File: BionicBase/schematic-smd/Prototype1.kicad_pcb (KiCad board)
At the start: 2 copper layers, 114 x 102 mm, 15 parts, among them J1 Bionic_ZIF_Socket_48pin, SW1 Tact_SW, U1 TXS0108EPW, U2 TXS0108EPW, U3 TXS0108EPW, U4 TXS0108EPW, U5 TXS0108EPW

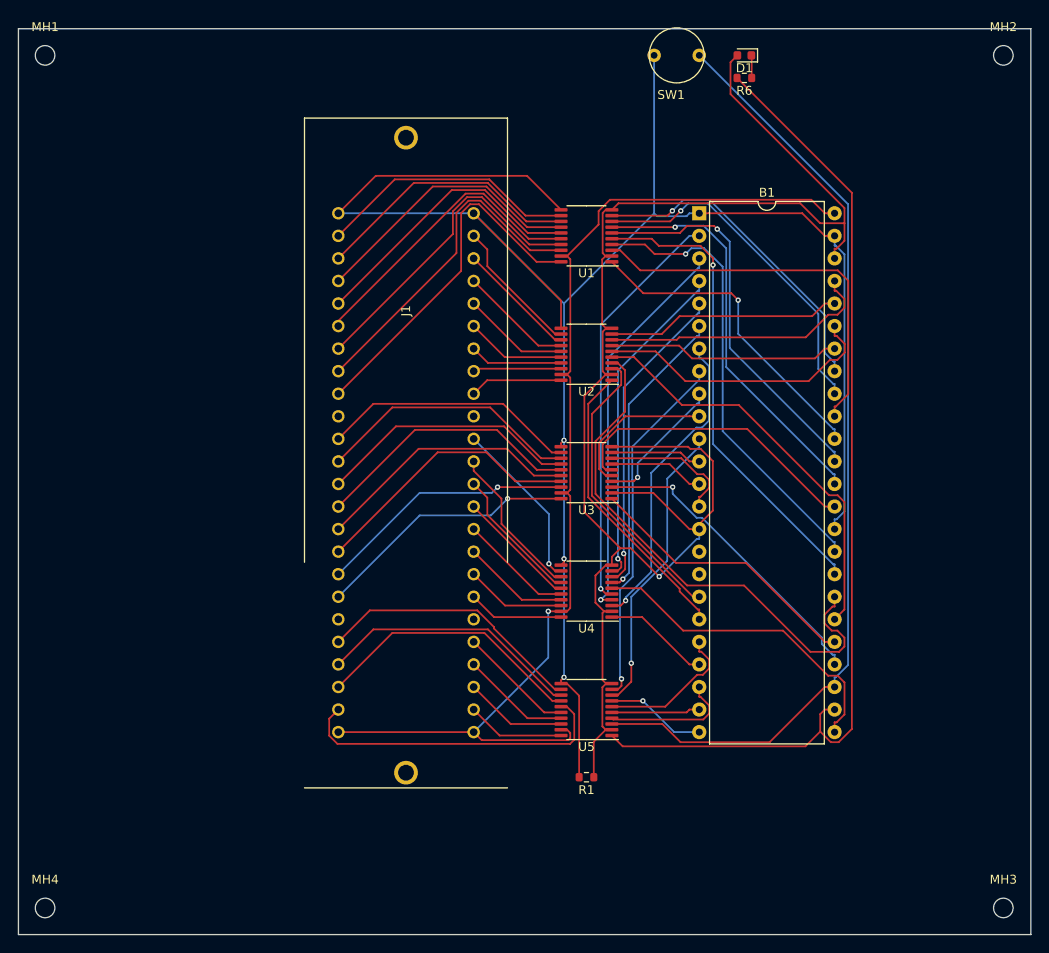
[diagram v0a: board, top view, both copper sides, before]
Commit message: [BionicBase] Add DC-DC Converter for +15V
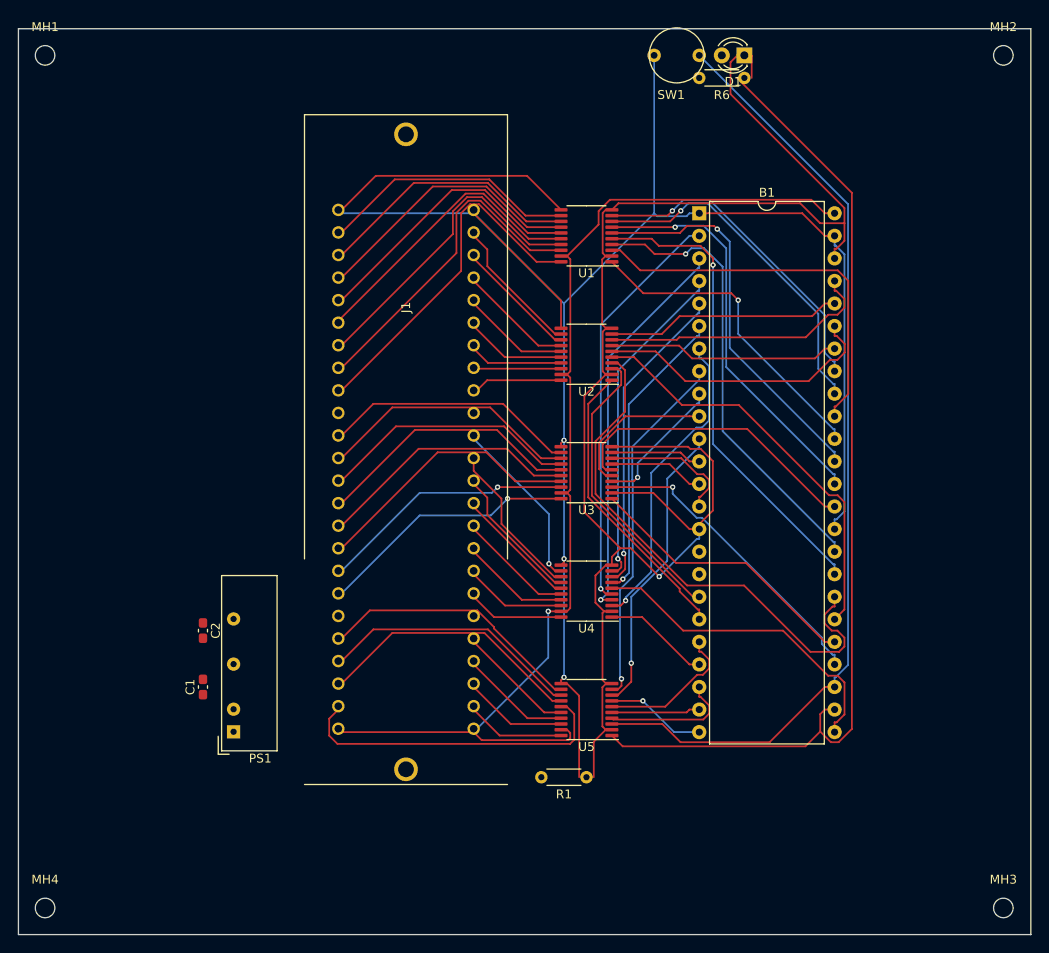
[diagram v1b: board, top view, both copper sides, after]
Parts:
- added C1: 2.2u, Capacitor_SMD:C_0603_1608Metric_Pad1.08x0.95mm_HandSolder, F.Cu at (93.4, 115.7)
- added C2: 1.0u, Capacitor_SMD:C_0603_1608Metric_Pad1.08x0.95mm_HandSolder, F.Cu at (93.4, 109.4)
- added PS1: MAU105, 0-LocalLibrary:Converter_DCDC_Minmax_MAU100_THT, F.Cu at (96.8, 120.8)
- D1: footprint LED_SMD:LED_0603_1608Metric -> LED_THT:LED_D3.0mm
- R1, R6: footprint Resistor_SMD:R_0603_1608Metric -> Resistor_THT:R_Axial_DIN0204_L3.6mm_D1.6mm_P5.08mm_Horizontal
- moved J1 0.38 mm to (116.2, 76.0)
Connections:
- net +3V3 renamed +3.3V
- J1 pad 19: unconnected-(J1-Pad19) -> /+15V
- J1 pad 30: unconnected-(J1-Pad30) -> /+15V
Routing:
- net (no net): track 0.00 -> 179.8 mm, vias 0 -> 1
- net +3.3V: track 177.2 -> 0.00 mm, vias 1 -> 0
- net Net-(D1-K): track 2.56 -> 0.00 mm
